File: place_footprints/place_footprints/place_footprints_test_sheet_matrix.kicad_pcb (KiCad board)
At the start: 2 copper layers, 64 parts

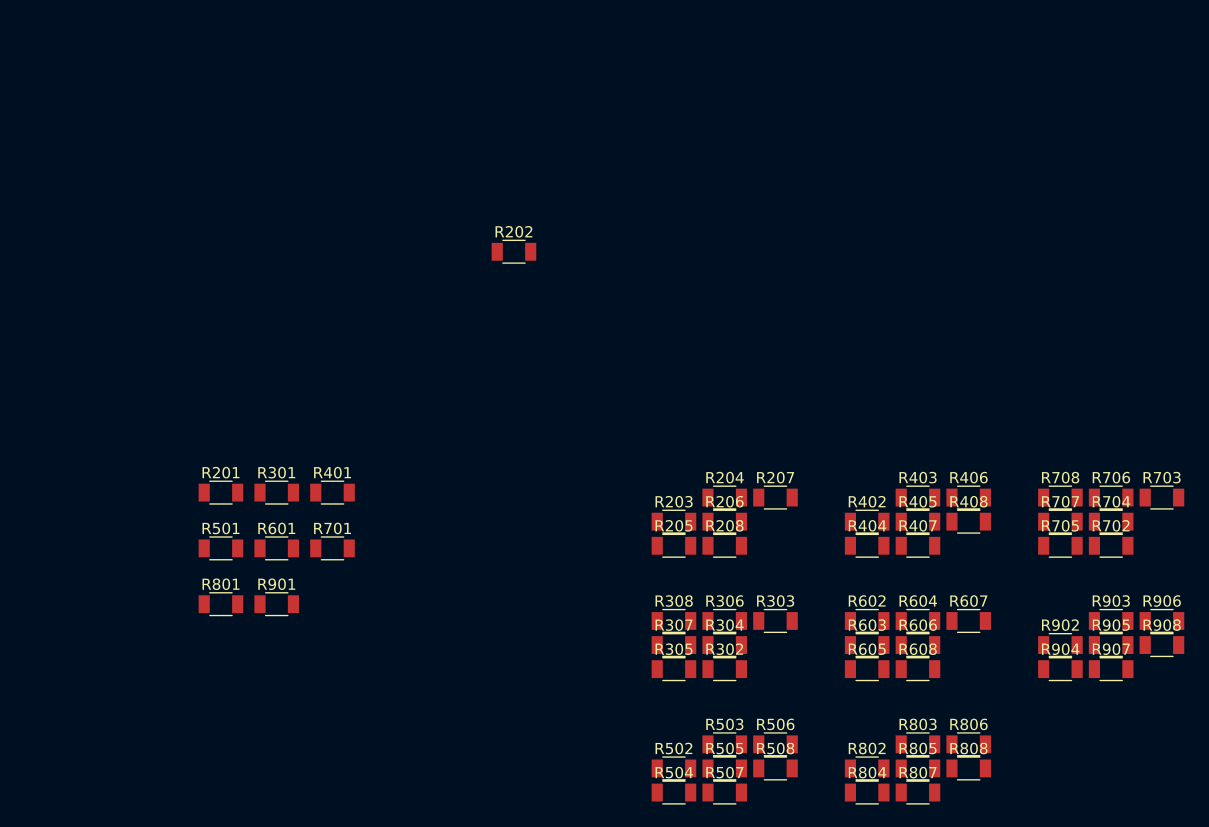
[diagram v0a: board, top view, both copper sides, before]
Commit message: Fixed circular placement
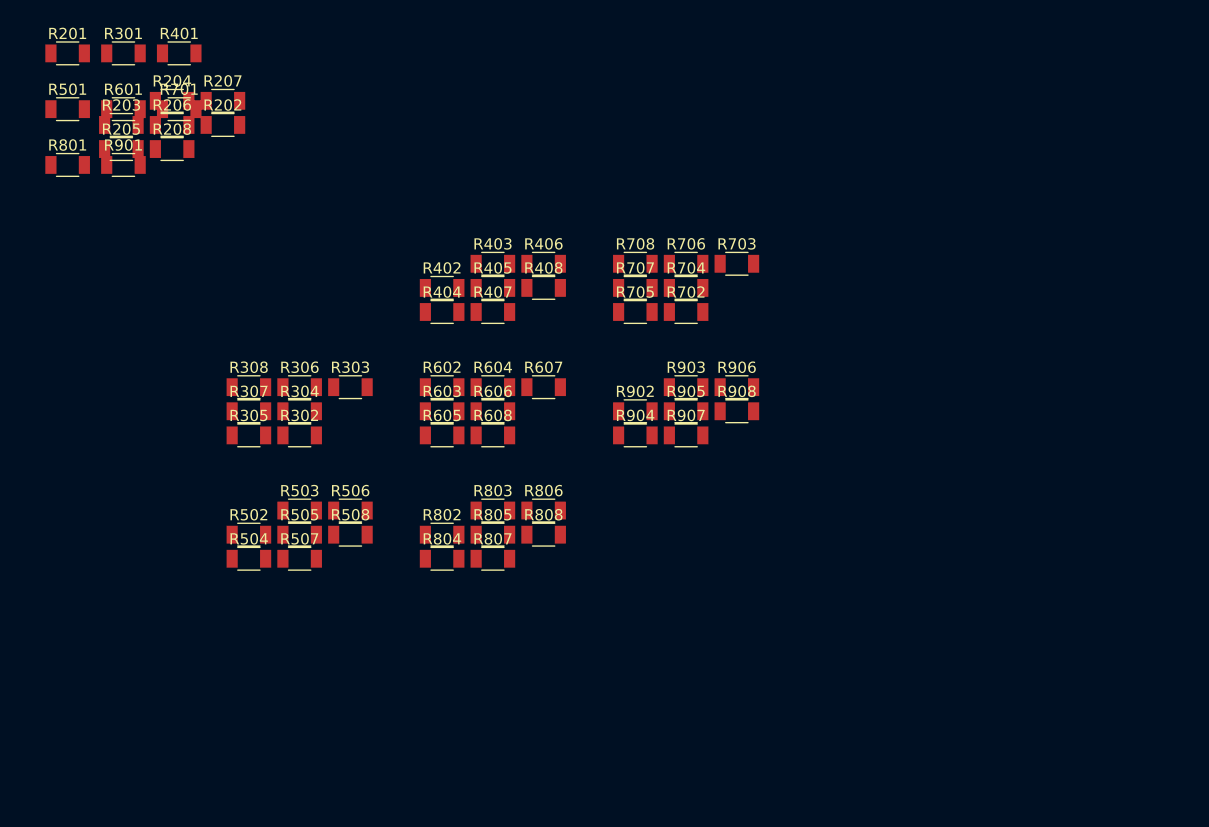
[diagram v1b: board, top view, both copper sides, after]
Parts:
- moved R204 61.0 mm to (53.2, 33.5)
- moved R206 61.0 mm to (53.2, 35.6)
- moved R208 61.0 mm to (53.2, 37.8)
- moved R207 61.0 mm to (57.7, 33.5)
- moved R203 61.0 mm to (48.6, 35.6)
- moved R205 61.0 mm to (48.6, 37.8)
- moved R302 43.5 mm to (64.6, 63.5)
- moved R303 43.5 mm to (69.2, 59.1)
- moved R304 43.5 mm to (64.6, 61.3)
- moved R306 43.5 mm to (64.6, 59.1)
- moved R402 43.5 mm to (77.4, 50.2)
- moved R404 43.5 mm to (77.4, 52.4)
- moved R503 43.5 mm to (64.6, 70.2)
- moved R505 43.5 mm to (64.6, 72.4)
- moved R506 43.5 mm to (69.2, 70.2)
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
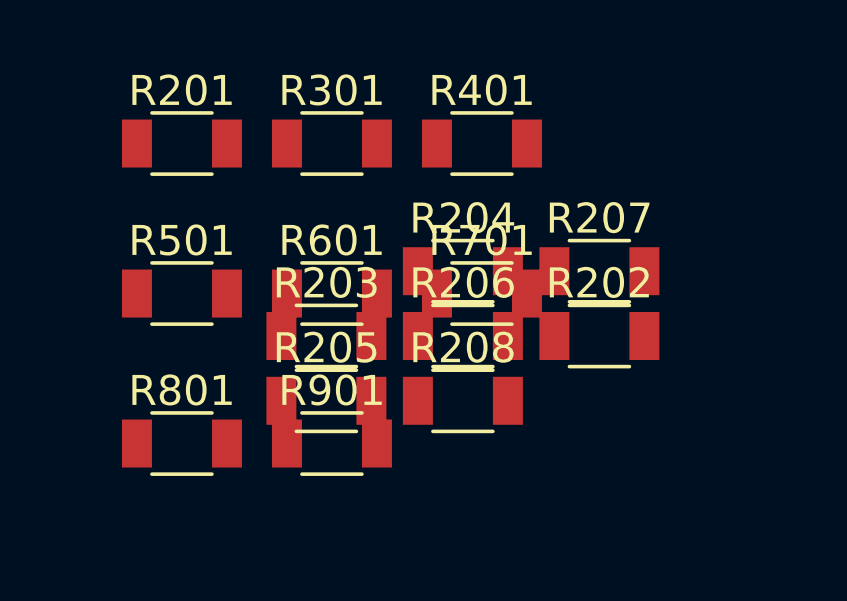
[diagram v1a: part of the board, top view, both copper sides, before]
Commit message: updated test cases
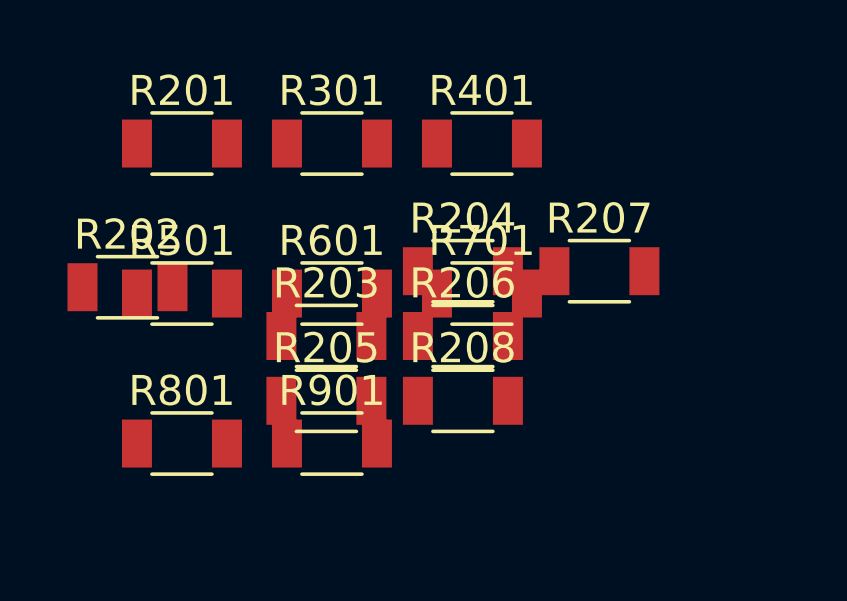
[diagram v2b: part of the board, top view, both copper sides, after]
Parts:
- moved R202 15.8 mm to (42.0, 34.0)
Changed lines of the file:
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@@
-(kicad_pcb (version 20171130) (host pcbnew "(5.0.2)-1")
+(kicad_pcb (version 20171130) (host pcbnew "(5.1.5-90-g5c7ac1bb7)-1")
   (general
     (thickness 1.6)
@@
     (zone_45_only no)
     (trace_min 0.2)
-    (segment_width 0.2)
-    (edge_width 0.15)
     (via_size 0.8)
     (via_drill 0.4)
@@
     (uvia_min_size 0.2)
     (uvia_min_drill 0.1)
+    (edge_width 0.15)
+    (segment_width 0.2)
     (pcb_text_width 0.3)
     (pcb_text_size 1.5 1.5)
@@
   )
   (module Passives:R1206M (layer F.Cu)
-    (at 57.730001 35.625001)
-    (descr "Capacitor SMD 1206, reflow soldering, AVX (see smccp.pdf)")
-    (tags "capacitor 1206")
+    (at 42 34)
+    (descr "Capacitor SMD 1206, reflow soldering, AVX (see smccp.pdf)")
+    (tags "capacitor 1206")
